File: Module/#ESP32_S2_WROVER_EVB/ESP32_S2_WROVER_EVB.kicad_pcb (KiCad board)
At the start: 2 copper layers, 90 parts, among them J1 CQ-USB-C16PSMT01, J2 microSD, J3 Motor, J4 ADC_IN1, J5 ADC_IN2, J6 ADC_REF, Q1 Q_NPN_BEC, Q2 Q_NPN_BEC, SW1 SW_Push, SW2 SW_Push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

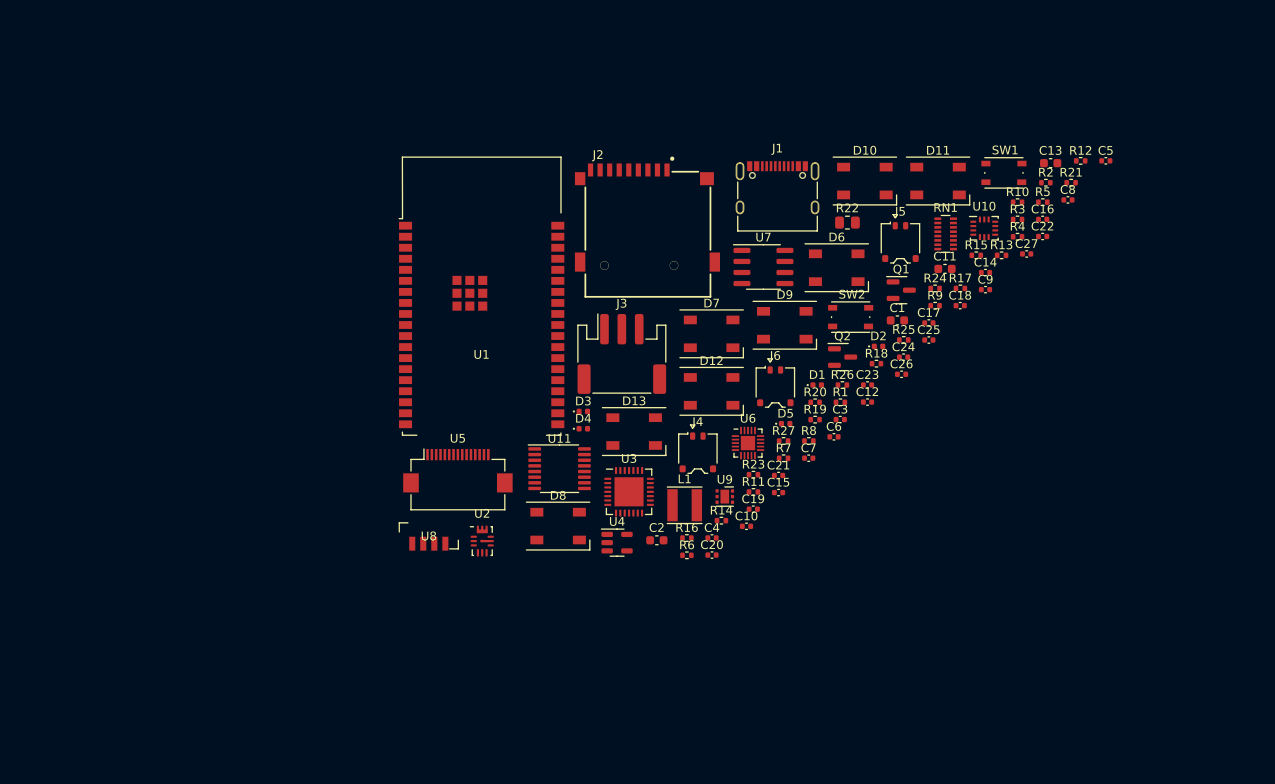
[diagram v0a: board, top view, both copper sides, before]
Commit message: update ESP-S2-Wrover module
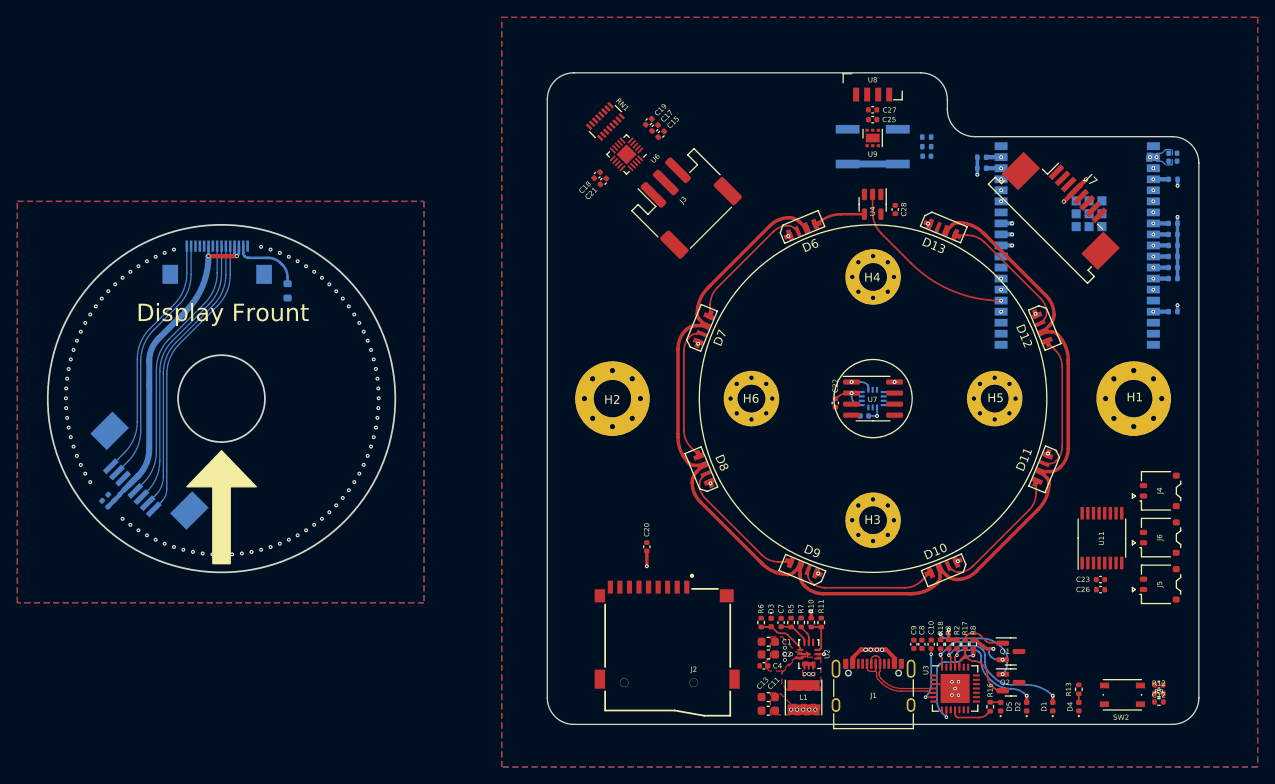
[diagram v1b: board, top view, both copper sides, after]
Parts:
- added C28: 1uF, Capacitor_SMD:C_0402_1005Metric, F.Cu at (172.6, 73.2)
- added H1: Solid, MountingHole:MountingHole_4.3mm_M4_Pad_Via, F.Cu at (200.0, 95.0)
- added H2: Solid, MountingHole:MountingHole_4.3mm_M4_Pad_Via, F.Cu at (140.0, 95.0)
- added H3: Motor, MountingHole:MountingHole_3.2mm_M3_Pad_Via, F.Cu at (170.0, 109.0)
- added H4: Motor, MountingHole:MountingHole_3.2mm_M3_Pad_Via, F.Cu at (170.0, 81.0)
- added H5: Motor, MountingHole:MountingHole_3.2mm_M3_Pad_Via, F.Cu at (184.0, 95.0)
- added H6: Motor, MountingHole:MountingHole_3.2mm_M3_Pad_Via, F.Cu at (156.0, 95.0)
- added J7: Screen_C, Connector_FFC-FPC:TE_84953-8_1x08-1MP_P1.0mm_Horizontal, F.Cu at (192.3, 72.7)
- added J8: Screen_C, Connector_FFC-FPC:TE_84953-8_1x08-1MP_P1.0mm_Horizontal, B.Cu at (86.0, 104.0)
- C14, C16, C24, C3, C5, C6, R1, R14, R15, R19, R20, R21, R23, R24, R25, R26, R27, R4, U1, U10, U5: moved to B.Cu
- D10, D11, D12, D13, D6, D7, D8, D9: footprint LED_SMD:LED_SK6812_PLCC4_5.0x5.0mm_P3.2mm -> lib:SK6812-4020
- J2: value microSD -> GCT_MEM2075-00-140-01-A
- R22: footprint Resistor_SMD:R_0805_2012Metric -> Resistor_SMD:R_0603_1608Metric; moved to B.Cu
- SW1: footprint Button_Switch_SMD:SW_Push_1P1T_NO_Vertical_Wuerth_434133025816 -> Button_Switch_SMD:SW_SPST_EVQP0; moved to B.Cu
- moved C16 111.9 mm to (82.3, 106.4), turned to 135 degrees
- moved C14 104.8 mm to (81.6, 107.1), turned to 135 degrees
- moved U8 72.7 mm to (170.0, 58.6)
- moved C13 70.9 mm to (157.9, 130.9), turned to 180 degrees
- moved U1 69.2 mm to (193.5, 77.5), turned to 180 degrees
- moved D4 65.4 mm to (193.7, 130.5), turned to 90 degrees
- moved R22 64.9 mm to (102.6, 82.6), turned to 90 degrees
- moved U11 62.9 mm to (196.3, 111.1), turned to 90 degrees
- moved R12 62.0 mm to (202.9, 128.9)
- moved J1 58.3 mm to (170.1, 129.2)
- moved R14 57.3 mm to (204.5, 85.0), turned to 180 degrees
- moved R5 56.4 mm to (160.6, 120.8), turned to 90 degrees
- moved R2 54.1 mm to (179.7, 123.3), turned to 90 degrees
- moved R10 53.9 mm to (162.9, 120.8), turned to -90 degrees
- moved C8 53.8 mm to (175.6, 123.3), turned to -90 degrees
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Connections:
- C14 pad 1: +3V3 -> /Screen_VCC
- C14 pad 2: GND -> /Screen_GND
- C16 pad 1: +3V3 -> /Screen_VCC
- C16 pad 2: GND -> /Screen_GND
- D10 pad 1: GND -> Net-(D10-Pad1)
- D10 pad 2: Net-(D10-Pad2) -> +5V
- D10 pad 3: +5V -> Net-(D10-Pad3)
- D10 pad 4: Net-(D10-Pad4) -> GND
- D11 pad 1: GND -> Net-(D10-Pad3)
- D11 pad 2: Net-(D10-Pad4) -> +5V
- D11 pad 3: +5V -> Net-(D11-Pad3)
- D11 pad 4: Net-(D11-Pad4) -> GND
- D12 pad 1: GND -> Net-(D11-Pad3)
- D12 pad 2: Net-(D11-Pad4) -> +5V
- D12 pad 3: +5V -> Net-(D12-Pad3)
- D12 pad 4: Net-(D12-Pad4) -> GND
- D13 pad 1: GND -> Net-(D12-Pad3)
- D13 pad 2: Net-(D12-Pad4) -> +5V
- D13 pad 3: +5V -> unconnected-(D13-Pad3)
- D13 pad 4: unconnected-(D13-Pad4) -> GND
- D6 pad 1: GND -> Net-(D6-Pad1)
- D6 pad 2: Net-(D6-Pad2) -> +5V
- D6 pad 3: +5V -> Net-(D6-Pad3)
- D6 pad 4: Net-(D6-Pad4) -> GND
- D7 pad 1: GND -> Net-(D6-Pad3)
- D7 pad 2: Net-(D6-Pad4) -> +5V
- D7 pad 3: +5V -> Net-(D7-Pad3)
- D7 pad 4: Net-(D7-Pad4) -> GND
- D8 pad 1: GND -> Net-(D7-Pad3)
- D8 pad 2: Net-(D7-Pad4) -> +5V
- D8 pad 3: +5V -> Net-(D8-Pad3)
- D8 pad 4: Net-(D8-Pad4) -> GND
- D9 pad 1: GND -> Net-(D8-Pad3)
- D9 pad 2: Net-(D8-Pad4) -> +5V
- D9 pad 3: +5V -> Net-(D10-Pad1)
- D9 pad 4: Net-(D10-Pad2) -> GND
- R22 pad 1: GND -> /Screen_GND
- R27 pad 1: DP_CS -> +3V3
- R27 pad 2: +3V3 -> DP_CS
- RN1 pad 1: TMC_UH -> TMC_VL
- RN1 pad 2: TMC_UL -> unconnected-(RN1-Pad2)
- RN1 pad 3: TMC_VH -> unconnected-(RN1-Pad3)
- RN1 pad 4: TMC_VL -> TMC_WL
- RN1 pad 5: TMC_WH -> TMC_UL
- RN1 pad 6: TMC_WL -> TMC_WH
- RN1 pad 7: unconnected-(RN1-Pad7) -> TMC_VH
- RN1 pad 8: unconnected-(RN1-Pad8) -> TMC_UH
- U4 pad 4: Net-(D6-Pad2) -> Net-(D6-Pad1)
- U5 pad 1: GND -> /Screen_GND
- U5 pad 10: +3V3 -> /Screen_VCC
- U5 pad 11: GND -> /Screen_GND
- U5 pad 14: ESP_I2C_SCL -> /Screen_TP_SCL
- U5 pad 15: ESP_I2C_SDA -> /Screen_TP_SDA
- U5 pad 3: +3V3 -> /Screen_VCC
- U5 pad 4: +3V3 -> /Screen_VCC
- U5 pad 5: ESP_SPI_MISO -> /Screen_DP_CMD
- U5 pad 6: DP_CS -> /Screen_DP_CS
- U5 pad 7: ESP_SPI_CLK -> /Screen_DP_CLK
- U5 pad 8: ESP_SPI_MOSI -> /Screen_DP_DATA
- U5 pad MP: GND -> /Screen_GND
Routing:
- net +5V: track 0.00 -> 160.8 mm, vias 0 -> 8
- net /Screen_VCC: track 0.00 -> 39.7 mm, vias 0 -> 2
- net /Screen_DP_CMD: track 0.00 -> 32.5 mm
- net /Screen_DP_CS: track 0.00 -> 31.8 mm
- net /Screen_DP_CLK: track 0.00 -> 31.1 mm
- net +3V3: track 0.00 -> 31.0 mm, vias 0 -> 22
- net /Screen_DP_DATA: track 0.00 -> 30.5 mm
- net /Screen_TP_SCL: track 0.00 -> 28.0 mm
- net /Screen_TP_SDA: track 0.00 -> 27.4 mm
- net String_LED: track 0.00 -> 21.0 mm, vias 0 -> 1
- net ESP_RX: track 0.00 -> 18.3 mm, vias 0 -> 3
- net Net-(D8-Pad3): track 0.00 -> 15.7 mm
- net Net-(D6-Pad3): track 0.00 -> 15.7 mm
- net Net-(D10-Pad3): track 0.00 -> 15.7 mm
- net Net-(D12-Pad3): track 0.00 -> 15.7 mm
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- added copper zone on B.Cu, net +3V3
- added copper zone on F.Cu, net +3V3
- added copper zone on In1.Cu, net +3V3
- added copper zone on F.Cu, net +5V
- added copper zone on B.Cu, net /Screen_GND
- added copper zone on F.Cu, net /Screen_GND
- added copper zone on B.Cu, net GND
- added copper zone on F.Cu, net GND
- added copper zone on F.Cu, net Net-(L1-Pad1)
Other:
- board outline added: 132.5 x 75 mm
- copper layers 2 -> 4
- board text added: "Display Frount"
